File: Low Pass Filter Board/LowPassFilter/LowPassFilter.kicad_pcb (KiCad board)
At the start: 4 copper layers, 40.9 x 18 mm, 6 parts

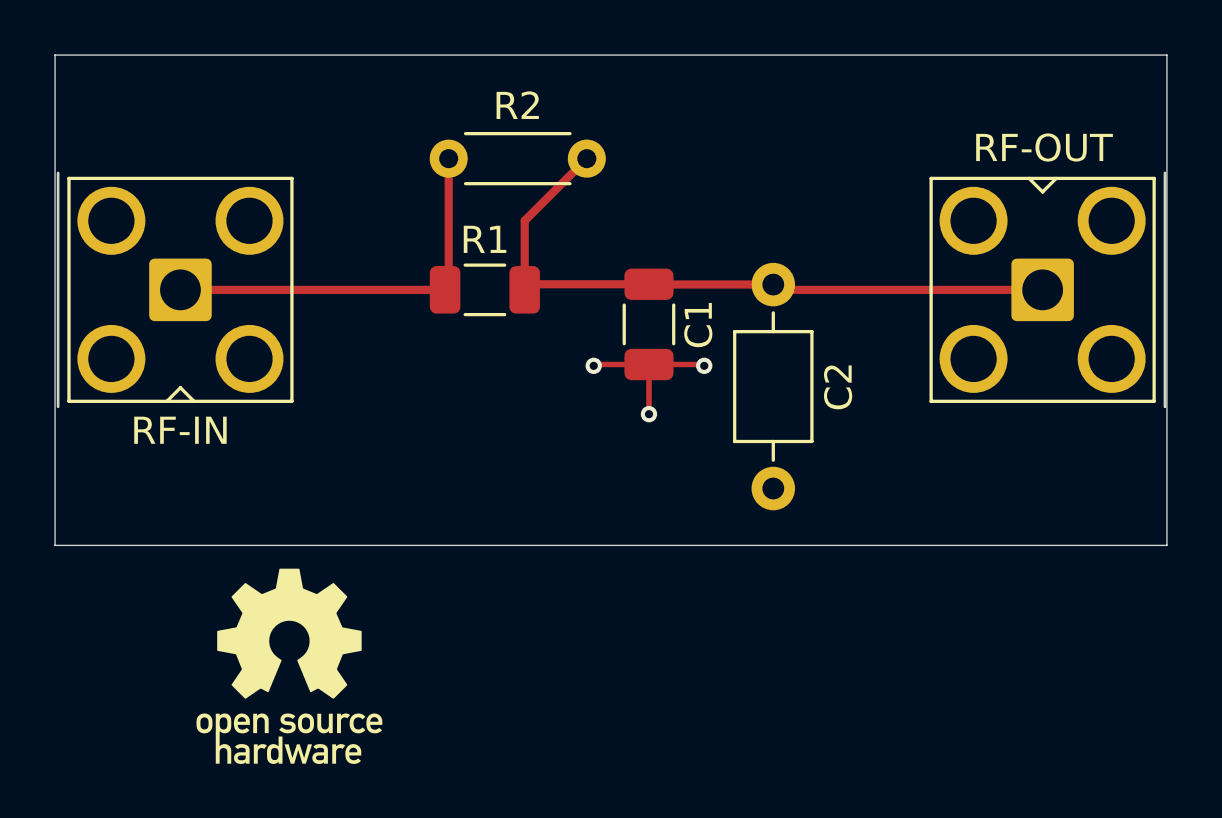
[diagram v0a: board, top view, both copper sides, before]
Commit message: Working on silkscreen and ordering
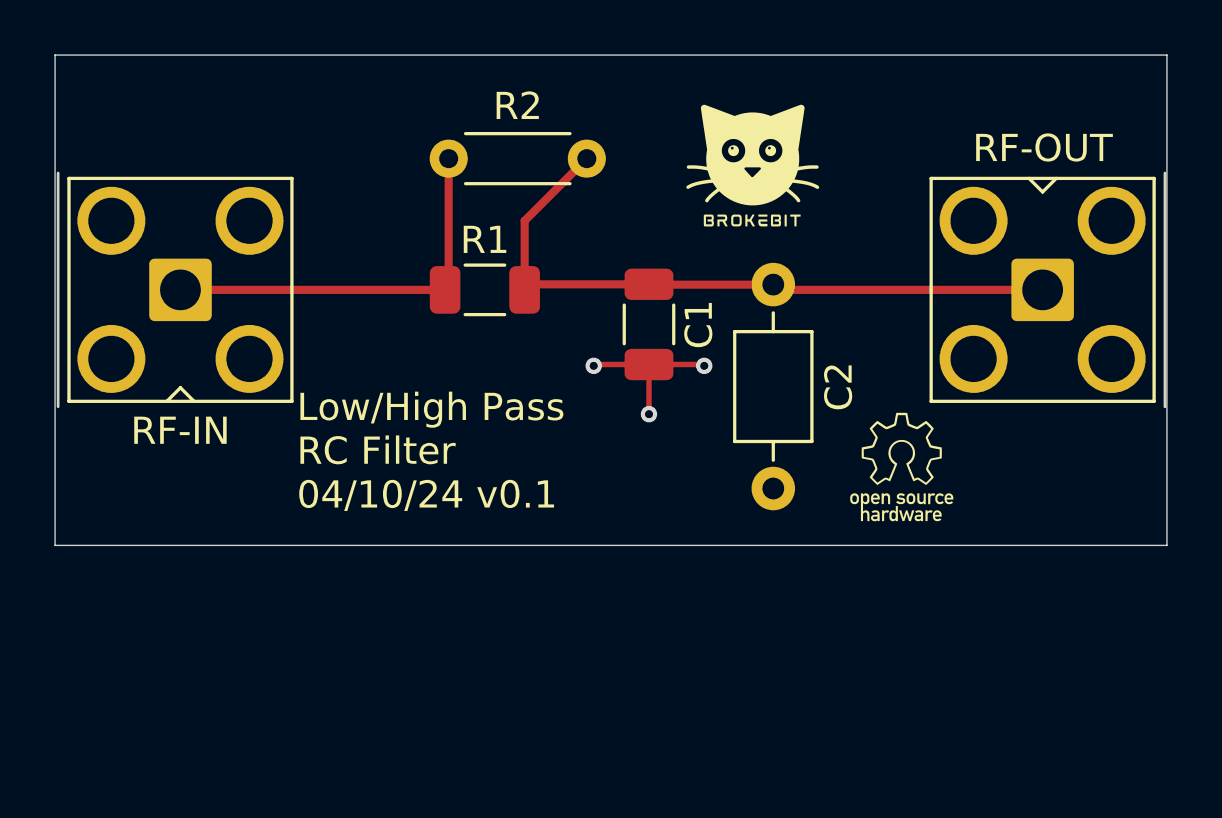
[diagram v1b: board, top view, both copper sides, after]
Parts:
- added G***: LOGO, LOGO, F.Cu at (153.4, 90.4)
- added G***: LOGO, LOGO, F.Cu at (159.0, 101.6)
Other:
- board text added: "Low/High Pass RC Filter 04/10/24 v0.1"
